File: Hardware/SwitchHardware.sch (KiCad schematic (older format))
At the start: 1 part

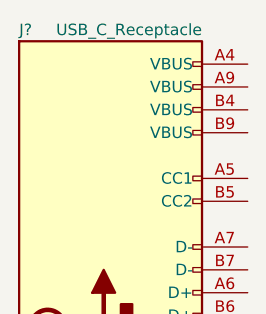
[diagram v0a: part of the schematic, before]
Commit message: Add typ c to pcb
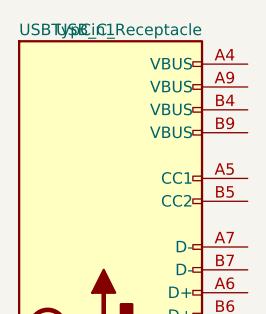
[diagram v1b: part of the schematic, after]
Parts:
- USBTypCin1: renamed from J?; footprint (none) -> Connectors_USB:USB_C_Receptacle_Amphenol_12401548E4-2A_CircularHoles
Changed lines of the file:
@@
 LIBS:contrib
 LIBS:valves
+LIBS:SwitchHardware-cache
 EELAYER 25 0
 EELAYER END
@@
 $EndDescr
 $Comp
-L USB_C_Receptacle J?
+L USB_C_Receptacle USBTypCin1
 U 1 1 5B141445
 P 1700 2500
-F 0 "J?" H 1300 3950 50  0000 L CNN
+F 0 "USBTypCin1" H 1300 3950 50  0000 L CNN
 F 1 "USB_C_Receptacle" H 2100 3950 50  0000 R CNN
-F 2 "" H 1850 2500 50  0001 C CNN
+F 2 "Connectors_USB:USB_C_Receptacle_Amphenol_12401548E4-2A_CircularHoles" H 1850 2500 50  0001 C CNN
 F 3 "" H 1850 2500 50  0001 C CNN
 	1    1700 2500
